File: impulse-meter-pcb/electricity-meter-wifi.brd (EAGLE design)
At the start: 34.3 x 68.8 mm, 14 parts, among them U2 MCP1316MT-29ME/OT

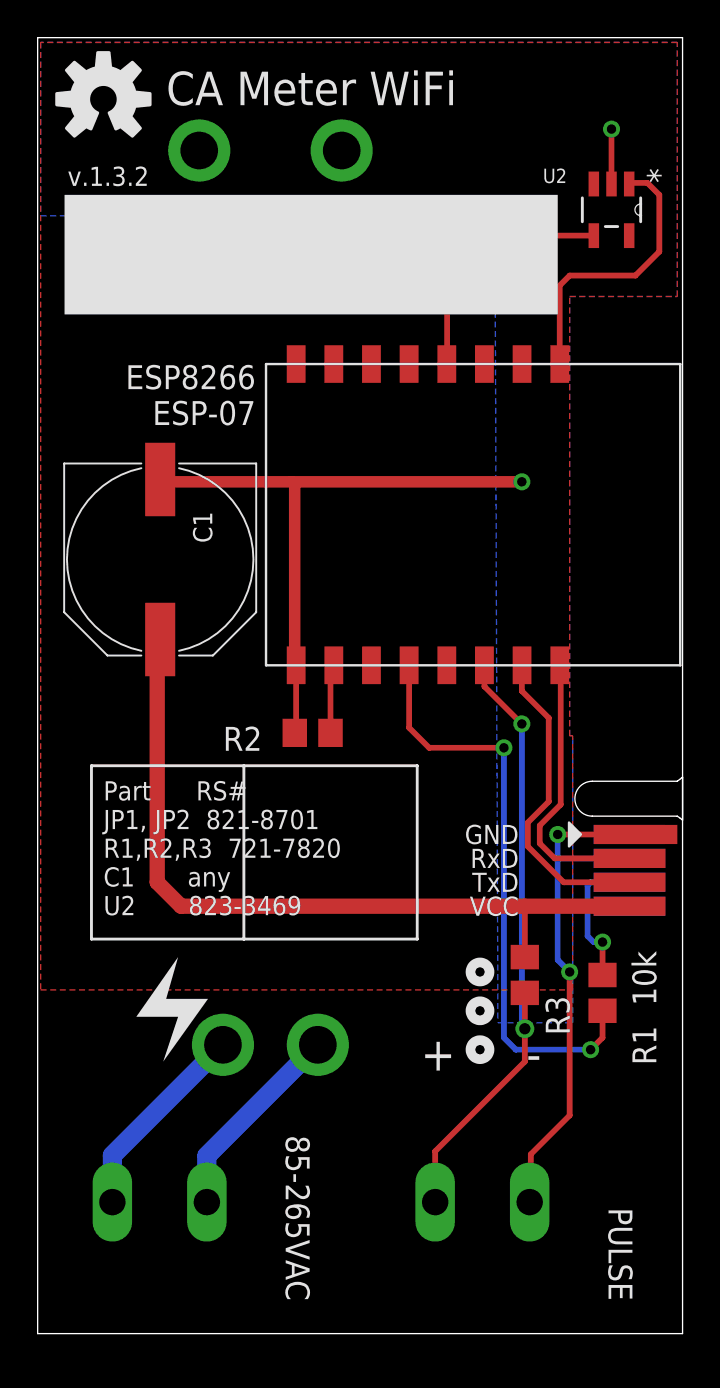
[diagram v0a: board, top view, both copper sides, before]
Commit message: pcb v1.3.4
added PE hole
rotated c1
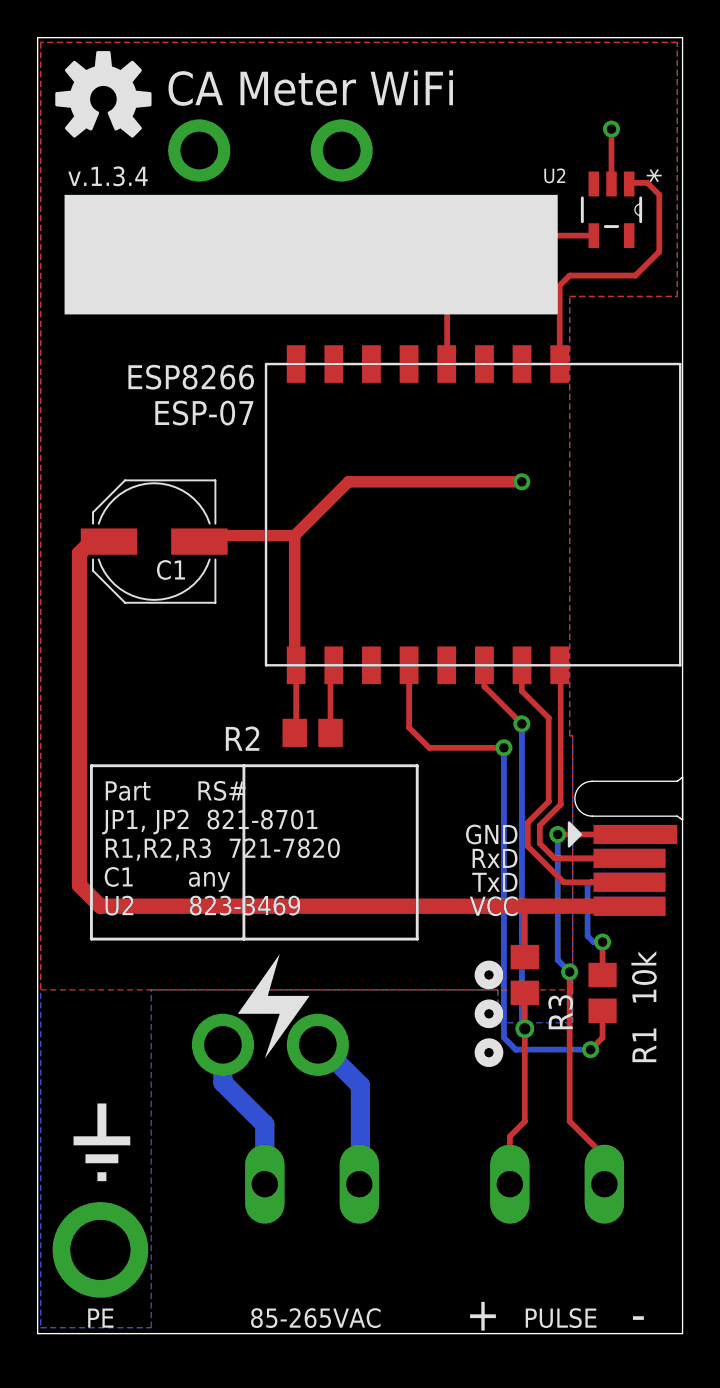
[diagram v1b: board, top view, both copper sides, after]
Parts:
- C1: device rcl:PANASONIC_G -> SparkFun-Capacitors:PANASONIC_D
- moved JP1 8.15 mm to (12.1, 7.94)
- moved JP2 4.08 mm to (25.1, 7.94)
- moved C1 1.00 mm to (6.19, 42.1), turned to 180 degrees
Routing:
- net 3.3V: track 41.3 -> 51.9 mm
- net GND: track 64.4 -> 59.5 mm, vias 4 -> 5
- net N$3: track 33.3 -> 30.7 mm
- net N$6: track 10.8 -> 8.32 mm
- net N$5: track 10.8 -> 8.42 mm
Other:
- board text added: "PE"
- board text added: "v.1.3.4"
- board text removed: "v.1.3.2"

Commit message: pcb: v.1.3.6
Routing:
- net GND: track 59.5 -> 45.3 mm
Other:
- board text added: "v.1.3.6"
- board text removed: "v.1.3.4"
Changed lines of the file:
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@@
 <text x="11.58875" y="48.26" size="1.27" layer="25" ratio="10" align="bottom-right">ESP8266
 ESP-07</text>
-<text x="1.5875" y="60.96" size="1.016" layer="25" ratio="15">v.1.3.4</text>
+<text x="1.5875" y="60.96" size="1.016" layer="25" ratio="15">v.1.3.6</text>
 <text x="3.4925" y="22.225" size="1.016" layer="25" font="fixed">Part      RS#
 JP1, JP2  821-8701
@@
 /nabovarme/electricity-meter-wifi</text>
 <text x="3.33375" y="0.3175" size="1.016" layer="25" ratio="15" rot="SR0" align="bottom-center">PE</text>
-<rectangle x1="1.905" y1="10.00125" x2="4.92125" y2="10.4775" layer="25"/>
-<rectangle x1="3.175" y1="8.09625" x2="3.65125" y2="8.5725" layer="25"/>
-<rectangle x1="2.54" y1="9.04875" x2="4.28625" y2="9.525" layer="25"/>
-<rectangle x1="2.54" y1="11.1125" x2="4.28625" y2="11.58875" layer="25" rot="R90"/>
+<rectangle x1="1.905" y1="12.54125" x2="4.92125" y2="13.0175" layer="25"/>
+<rectangle x1="3.175" y1="10.63625" x2="3.65125" y2="11.1125" layer="25"/>
+<rectangle x1="2.54" y1="11.58875" x2="4.28625" y2="12.065" layer="25"/>
+<rectangle x1="2.54" y1="13.6525" x2="4.28625" y2="14.12875" layer="25" rot="R90"/>
 </plain>
 <attributes>
@@
 <element name="R3" library="rcl" package="R0805" value="10k" x="25.87625" y="19.05" smashed="yes" rot="R270">
 <attribute name="NAME" x="27.14625" y="18.0975" size="1.27" layer="25" rot="R270"/>
-<attribute name="VALUE" x="26.9875" y="23.1775" size="1.27" layer="27" rot="R270"/>
+<attribute name="VALUE" x="26.9875" y="23.1775" size="1.27" layer="25" rot="R270"/>
 </element>
 <element name="R2" library="rcl" package="R0805" value="10k" x="14.605" y="31.90875" smashed="yes">
 <attribute name="NAME" x="9.8425" y="30.95625" size="1.27" layer="25"/>
-<attribute name="VALUE" x="17.145" y="30.95625" size="1.27" layer="27"/>
+<attribute name="VALUE" x="17.145" y="30.95625" size="1.27" layer="25"/>
 </element>
 <element name="U2" library="Microchip_By_element14_Batch_1" package="SOT95P270X145-5N" value="MCP1316MT-29ME/OT" x="30.48" y="59.69" smashed="yes" rot="R270">
@@
 <attribute name="OC_FARNELL" value="1332071" x="30.48" y="59.69" size="1.778" layer="27" rot="R270" display="off"/>
 <attribute name="NAME" x="28.1178" y="61.1124" size="0.762" layer="25" ratio="12" rot="SR0" align="bottom-right"/>
-<attribute name="VALUE" x="32.3215" y="62.42685" size="0.762" layer="27" ratio="12" rot="SR0" align="bottom-right"/>
+<attribute name="VALUE" x="32.3215" y="62.42685" size="0.762" layer="25" ratio="12" rot="SR0" align="bottom-right"/>
 </element>
 </elements>
@@
 <via x="27.6225" y="26.51125" extent="1-16" drill="0.5"/>
 <wire x1="13.6525" y1="35.575" x2="13.73" y2="35.4975" width="0.8128" layer="1"/>
-<via x="25.7175" y="45.24375" extent="1-16" drill="0.5"/>
+<via x="11.27125" y="42.38625" extent="1-16" drill="0.5"/>
 <via x="28.2575" y="19.20875" extent="1-16" drill="0.5"/>
 <contactref element="JP2" pad="2"/>
@@
 <wire x1="30.1625" y1="9.36625" x2="30.1625" y2="7.9975" width="0.3048" layer="1"/>
 <wire x1="30.1625" y1="7.9975" x2="30.1025" y2="7.9375" width="0.3048" layer="1"/>
-<wire x1="13.6525" y1="35.575" x2="13.6525" y2="42.38625" width="0.6096" layer="1"/>
-<wire x1="13.6525" y1="42.38625" x2="16.51" y2="45.24375" width="0.6096" layer="1"/>
-<wire x1="16.51" y1="45.24375" x2="25.7175" y2="45.24375" width="0.6096" layer="1"/>
-<wire x1="13.6525" y1="42.38625" x2="8.90875" y2="42.38625" width="0.6096" layer="1"/>
 <wire x1="8.90875" y1="42.38625" x2="8.59125" y2="42.06875" width="0.6096" layer="1"/>
-<via x="3.33375" y="4.445" extent="1-16" drill="3.2" diameter="5.08"/>
+<via x="3.33375" y="6.985" extent="1-16" drill="3.2" diameter="5.08"/>
+<wire x1="8.90875" y1="42.38625" x2="12.065" y2="42.38625" width="0.6096" layer="1"/>
+<wire x1="12.065" y1="42.38625" x2="13.6525" y2="40.79875" width="0.6096" layer="1"/>
+<wire x1="13.6525" y1="40.79875" x2="13.6525" y2="35.575" width="0.6096" layer="1"/>
+<wire x1="11.27125" y1="42.38625" x2="12.065" y2="42.38625" width="0" layer="19" extent="1-1"/>
 </signal>
 <signal name="3.3V">
@@
 <wire x1="25.7175" y1="32.385" x2="25.7175" y2="16.35125" width="0.3048" layer="16"/>
 <wire x1="25.7175" y1="16.35125" x2="25.87625" y2="16.1925" width="0.3048" layer="16"/>
-<via x="25.87625" y="16.1925" extent="1-16" drill="0.6"/>
+<via x="25.87625" y="16.1925" extent="1-16" drill="0.5"/>
 <wire x1="25.87625" y1="16.1925" x2="25.87625" y2="11.27125" width="0.3048" layer="1"/>
 <wire x1="25.87625" y1="11.27125" x2="25.0825" y2="10.4775" width="0.3048" layer="1"/>

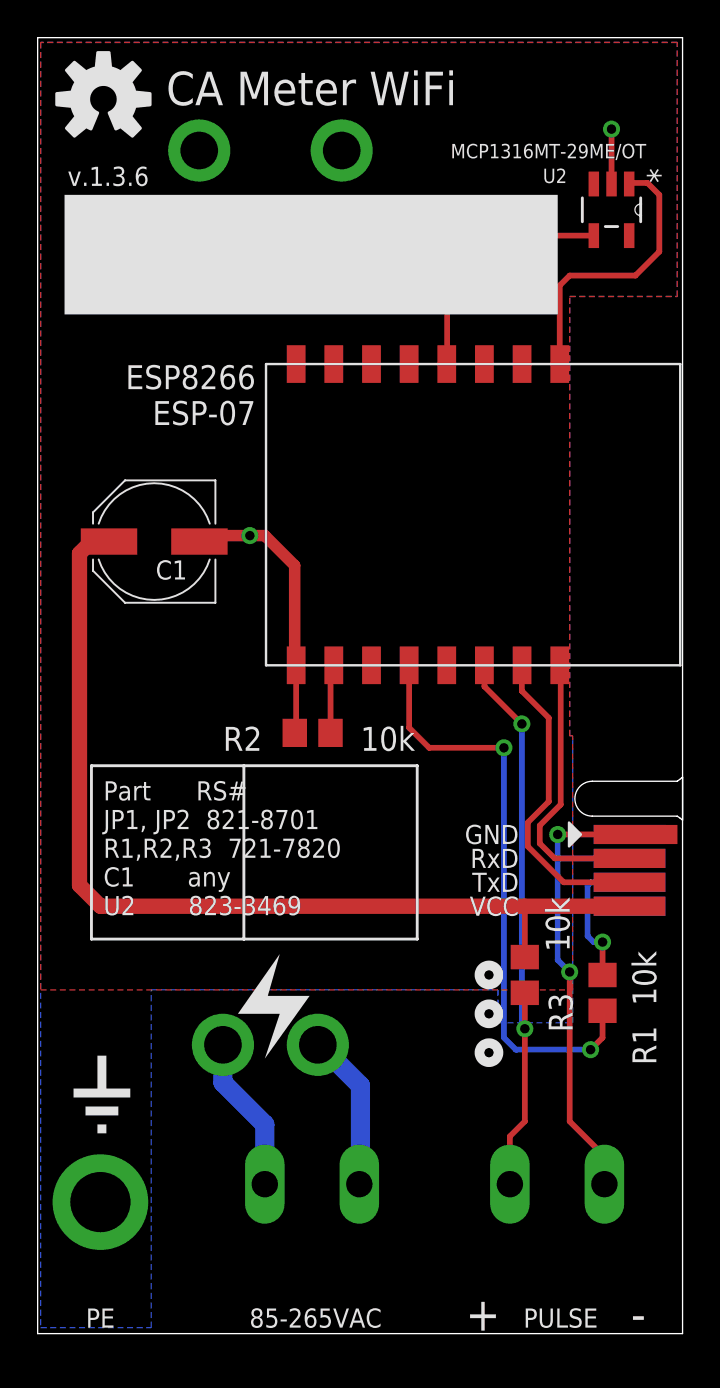
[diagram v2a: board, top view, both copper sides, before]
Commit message: PCB: v.1.4.1 Added FeRAM
+ docs
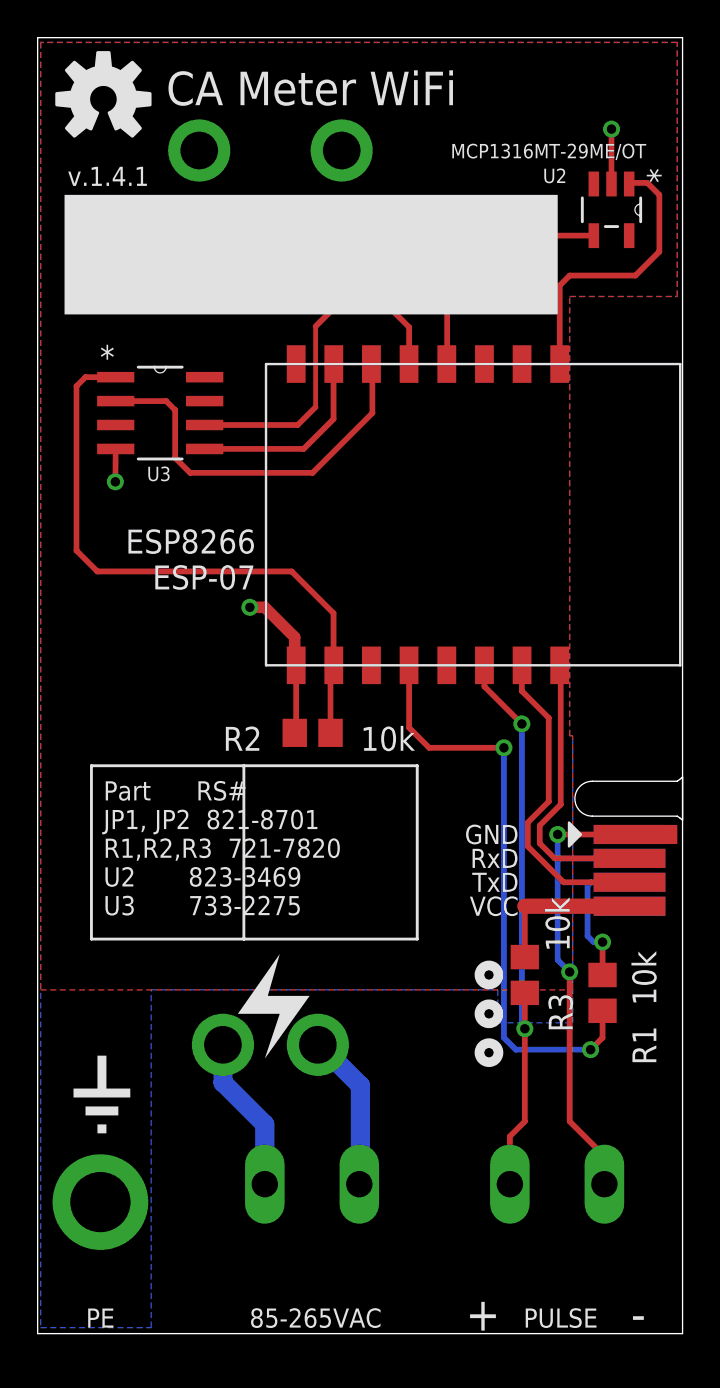
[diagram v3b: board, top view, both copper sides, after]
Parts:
- removed C1: (no value), SparkFun-Capacitors:PANASONIC_D
- added U3: FM25L16B, Microchip_By_element14_Batch_1:SOIC127P600X175-8N
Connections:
- new net N$10: ESP8266_ESP-07.GPIO12, U3.2
- new net N$12: ESP8266_ESP-07.GPIO13, U3.5
- new net N$13: ESP8266_ESP-07.GPIO14, U3.6
- net 3.3V: now also U3.3, U3.7, U3.8; no longer C1.+
- net GND: now also U3.4; no longer C1.-
- net N$7: now also U3.1
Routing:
- net 3.3V: track 51.9 -> 8.26 mm
- net N$7: track 3.66 -> 32.5 mm
- net N$10: track 0.00 -> 20.6 mm
- net N$13: track 0.00 -> 18.3 mm
- net N$12: track 0.00 -> 10.4 mm
- net GND: track 45.3 -> 40.4 mm, vias 5 -> 6
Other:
- board text added: "Part RS# JP1, JP2 821-8701 R1,R2,R3 721-7820 U2 823-3469 U3 733-2275"
- board text added: "v.1.4.1"
- board text removed: "Part RS# JP1, JP2 821-8701 R1,R2,R3 721-7820 C1 any U2 823-3469"
- board text removed: "v.1.3.6"
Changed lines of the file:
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@@
 <text x="25.55875" y="23.97125" size="1.016" layer="25" rot="R180" align="center-left">TxD</text>
 <text x="25.55875" y="25.24125" size="1.016" layer="25" rot="R180" align="center-left">RxD</text>
-<text x="11.58875" y="48.26" size="1.27" layer="25" ratio="10" align="bottom-right">ESP8266
+<text x="11.58875" y="39.52875" size="1.27" layer="25" ratio="10" align="bottom-right">ESP8266
 ESP-07</text>
-<text x="1.5875" y="60.96" size="1.016" layer="25" ratio="15">v.1.3.6</text>
+<text x="1.5875" y="60.96" size="1.016" layer="25" ratio="15">v.1.4.1</text>
 <text x="3.4925" y="22.225" size="1.016" layer="25" font="fixed">Part      RS#
 JP1, JP2  821-8701
 R1,R2,R3  721-7820
-C1       any
-U2       823-3469</text>
+U2       823-3469
+U3       733-2275</text>
 <wire x1="2.8575" y1="30.1625" x2="10.95375" y2="30.1625" width="0.1524" layer="25"/>
 <wire x1="10.95375" y1="30.1625" x2="20.16125" y2="30.1625" width="0.1524" layer="25"/>
@@
 <element name="JP1" library="SparkFun (old)" package="1X02_LONGPADS" value="" x="12.065" y="7.9375" smashed="yes"/>
 <element name="JP2" library="SparkFun (old)" package="1X02_LONGPADS" value="" x="25.0825" y="7.9375" smashed="yes"/>
-<element name="C1" library="SparkFun-Capacitors" package="PANASONIC_D" value="" x="6.19125" y="42.06875" rot="R180"/>
 <element name="U$1" library="con-pcb-slot" package="CONN_SLOT_MINIMAL" value="CON-PCB-SLOT-0.05MINIMAL" x="31.714440625" y="24.60625" smashed="yes" rot="R90"/>
 <element name="R3" library="rcl" package="R0805" value="10k" x="25.87625" y="19.05" smashed="yes" rot="R270">
@@
 <attribute name="NAME" x="28.1178" y="61.1124" size="0.762" layer="25" ratio="12" rot="SR0" align="bottom-right"/>
 <attribute name="VALUE" x="32.3215" y="62.42685" size="0.762" layer="25" ratio="12" rot="SR0" align="bottom-right"/>
+</element>
+<element name="U3" library="Microchip_By_element14_Batch_1" package="SOIC127P600X175-8N" value="FM25L16B" x="6.50875" y="48.895" smashed="yes">
+<attribute name="PACKAGE" value="SOIC-8" x="6.50875" y="48.895" size="1.778" layer="27" display="off"/>
+<attribute name="OC_NEWARK" value="72J3627" x="6.50875" y="48.895" size="1.778" layer="27" display="off"/>
+<attribute name="MPN" value="25AA020A-I/SN" x="6.50875" y="48.895" size="1.778" layer="27" display="off"/>
+<attribute name="SUPPLIER" value="MICROCHIP" x="6.50875" y="48.895" size="1.778" layer="27" display="off"/>
+<attribute name="OC_FARNELL" value="1331343" x="6.50875" y="48.895" size="1.778" layer="27" display="off"/>
+<attribute name="NAME" x="5.79755" y="45.28185" size="0.762" layer="25" ratio="12" rot="SR0"/>
+<attribute name="VALUE" x="4.9149" y="51.77155" size="0.762" layer="27" ratio="12" rot="SR0"/>
 </element>
 </elements>
@@
 <contactref element="ESP8266_ESP-07" pad="GND"/>
 <contactref element="GND" pad="1"/>
-<contactref element="C1" pad="-"/>
 <via x="27.6225" y="26.51125" extent="1-16" drill="0.5"/>
 <wire x1="13.6525" y1="35.575" x2="13.73" y2="35.4975" width="0.8128" layer="1"/>
-<via x="11.27125" y="42.38625" extent="1-16" drill="0.5"/>
+<via x="11.27125" y="38.57625" extent="1-16" drill="0.5"/>
 <via x="28.2575" y="19.20875" extent="1-16" drill="0.5"/>
 <contactref element="JP2" pad="2"/>
@@
 <wire x1="30.1625" y1="9.36625" x2="30.1625" y2="7.9975" width="0.3048" layer="1"/>
 <wire x1="30.1625" y1="7.9975" x2="30.1025" y2="7.9375" width="0.3048" layer="1"/>
-<wire x1="8.90875" y1="42.38625" x2="8.59125" y2="42.06875" width="0.6096" layer="1"/>
 <via x="3.33375" y="6.985" extent="1-16" drill="3.2" diameter="5.08"/>
-<wire x1="8.90875" y1="42.38625" x2="12.065" y2="42.38625" width="0.6096" layer="1"/>
-<wire x1="12.065" y1="42.38625" x2="13.6525" y2="40.79875" width="0.6096" layer="1"/>
-<wire x1="13.6525" y1="40.79875" x2="13.6525" y2="35.575" width="0.6096" layer="1"/>
-<wire x1="11.27125" y1="42.38625" x2="12.065" y2="42.38625" width="0" layer="19" extent="1-1"/>
+<wire x1="12.065" y1="38.57625" x2="13.6525" y2="36.98875" width="0.6096" layer="1"/>
+<wire x1="13.6525" y1="36.98875" x2="13.6525" y2="35.575" width="0.6096" layer="1"/>
+<contactref element="U3" pad="4"/>
+<wire x1="12.065" y1="38.57625" x2="11.27125" y2="38.57625" width="0.6096" layer="1"/>
+<wire x1="4.14655" y1="46.99" x2="4.1275" y2="45.24375" width="0.3048" layer="1"/>
+<via x="4.1275" y="45.24375" extent="1-16" drill="0.5"/>
 </signal>
 <signal name="3.3V">
@@
 <contactref element="ESP8266_ESP-07" pad="VCC"/>
 <contactref element="3.3V" pad="1"/>
-<contactref element="C1" pad="+"/>
 <contactref element="U$1" pad="4"/>
-<wire x1="3.33375" y1="22.70125" x2="25.87625" y2="22.70125" width="0.8128" layer="1"/>
 <contactref element="R3" pad="1"/>
 <wire x1="25.87625" y1="22.70125" x2="31.439440625" y2="22.70125" width="0.8128" layer="1"/>
 <wire x1="25.87625" y1="22.70125" x2="25.87625" y2="20" width="0.3048" layer="1"/>
 <contactref element="U2" pad="5"/>
-<wire x1="3.81" y1="42.05" x2="3.79125" y2="42.06875" width="0.8128" layer="1"/>
-<wire x1="3.33375" y1="22.70125" x2="2.2225" y2="23.8125" width="0.8128" layer="1"/>
-<wire x1="2.2225" y1="23.8125" x2="2.2225" y2="41.43375" width="0.8128" layer="1"/>
-<wire x1="2.2225" y1="41.43375" x2="2.8575" y2="42.06875" width="0.8128" layer="1"/>
-<wire x1="2.8575" y1="42.06875" x2="3.79125" y2="42.06875" width="0.8128" layer="1"/>
+<contactref element="U3" pad="8"/>
+<contactref element="U3" pad="3"/>
+<contactref element="U3" pad="7"/>
 </signal>
 <signal name="N$11">
@@
 <wire x1="15.555" y1="31.90875" x2="15.555" y2="35.3225" width="0.3048" layer="1"/>
 <wire x1="15.555" y1="35.3225" x2="15.73" y2="35.4975" width="0.3048" layer="1"/>
-</signal>
-<signal name="VCC">
+<contactref element="U3" pad="1"/>
+<wire x1="4.14655" y1="50.8" x2="2.54" y2="50.8" width="0.3048" layer="1"/>
+<wire x1="2.54" y1="50.8" x2="2.06375" y2="50.32375" width="0.3048" layer="1"/>
+<wire x1="2.06375" y1="50.32375" x2="2.06375" y2="41.5925" width="0.3048" layer="1"/>
+<wire x1="2.06375" y1="41.5925" x2="3.175" y2="40.48125" width="0.3048" layer="1"/>
+<wire x1="3.175" y1="40.48125" x2="13.49375" y2="40.48125" width="0.3048" layer="1"/>
+<wire x1="13.49375" y1="40.48125" x2="15.71625" y2="38.25875" width="0.3048" layer="1"/>
+<wire x1="15.71625" y1="38.25875" x2="15.71625" y2="35.51125" width="0.3048" layer="1"/>
+<wire x1="15.71625" y1="35.51125" x2="15.73" y2="35.4975" width="0.3048" layer="1"/>
 </signal>
 <signal name="N$8">
@@
 <wire x1="21.74875" y1="51.51625" x2="21.73" y2="51.4975" width="0.3048" layer="1"/>
 </signal>
+<signal name="N$10">
+<contactref element="U3" pad="2"/>
+<contactref element="ESP8266_ESP-07" pad="GPIO12"/>
+<wire x1="14.605" y1="45.72" x2="8.09625" y2="45.72" width="0.3048" layer="1"/>
+<wire x1="8.09625" y1="45.72" x2="7.3025" y2="46.51375" width="0.3048" layer="1"/>
+<wire x1="7.3025" y1="46.51375" x2="7.3025" y2="49.05375" width="0.3048" layer="1"/>
+<wire x1="7.3025" y1="49.05375" x2="6.82625" y2="49.53" width="0.3048" layer="1"/>
+<wire x1="6.82625" y1="49.53" x2="4.14655" y2="49.53" width="0.3048" layer="1"/>
+<wire x1="14.605" y1="45.72" x2="17.78" y2="48.895" width="0.3048" layer="1"/>
+<wire x1="17.78" y1="48.895" x2="17.78" y2="51.4475" width="0.3048" layer="1"/>
+<wire x1="17.78" y1="51.4475" x2="17.73" y2="51.4975" width="0.3048" layer="1"/>
+</signal>
+<signal name="N$12">
+<contactref element="U3" pad="5"/>
+<contactref element="ESP8266_ESP-07" pad="GPIO13"/>
+<wire x1="8.87095" y1="46.99" x2="14.12875" y2="46.99" width="0.3048" layer="1"/>
+<wire x1="14.12875" y1="46.99" x2="15.71625" y2="48.5775" width="0.3048" layer="1"/>
+<wire x1="15.71625" y1="48.5775" x2="15.71625" y2="51.48375" width="0.3048" layer="1"/>
+<wire x1="15.71625" y1="51.48375" x2="15.73" y2="51.4975" width="0.3048" layer="1"/>
+</signal>
+<signal name="N$13">
+<contactref element="U3" pad="6"/>
+<contactref element="ESP8266_ESP-07" pad="GPIO14"/>
+<wire x1="19.73" y1="51.4975" x2="19.73" y2="53.45375" width="0.3048" layer="1"/>
+<wire x1="8.87095" y1="48.26" x2="13.81125" y2="48.26" width="0.3048" layer="1"/>
+<wire x1="13.81125" y1="48.26" x2="14.76375" y2="49.2125" width="0.3048" layer="1"/>
+<wire x1="14.76375" y1="49.2125" x2="14.76375" y2="53.49875" width="0.254" layer="1"/>
+<wire x1="14.76375" y1="53.49875" x2="15.71625" y2="54.45125" width="0.3048" layer="1"/>
+<wire x1="15.71625" y1="54.45125" x2="18.7325" y2="54.45125" width="0.3048" layer="1"/>
+<wire x1="18.7325" y1="54.45125" x2="19.73" y2="53.45375" width="0.3048" layer="1"/>
+</signal>
 </signals>
